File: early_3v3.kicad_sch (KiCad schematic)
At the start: 6 parts, among them U11 SE8633K2-HF

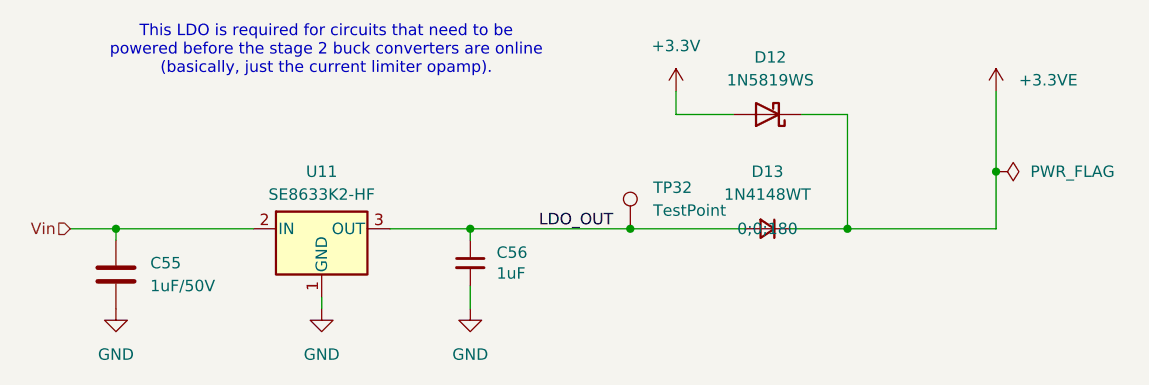
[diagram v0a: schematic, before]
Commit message: Nailed the current limiter design
Also added more GND test pads
Also fixed the MCU I2C pinout
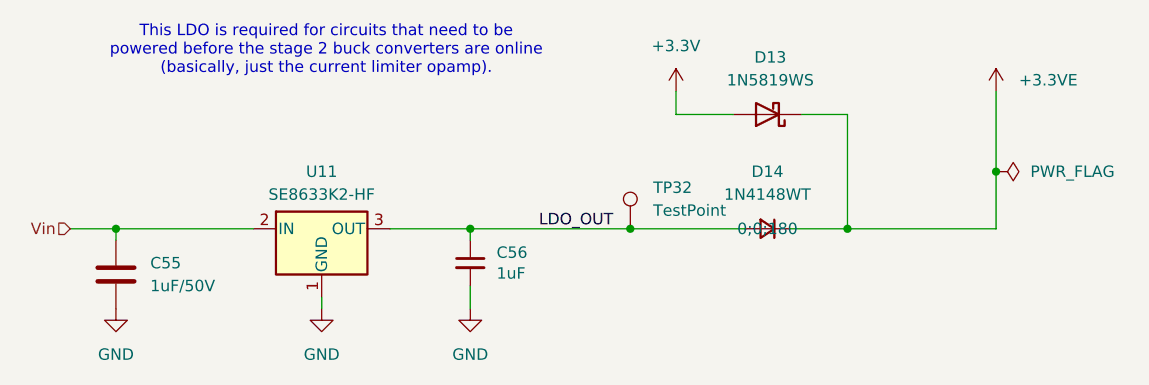
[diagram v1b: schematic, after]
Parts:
- renumbered D12 to D13, D13 to D14
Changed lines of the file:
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@@
 		(dnp no)
 		(fields_autoplaced yes)
-		(property "Reference" "D12"
+		(property "Reference" "D13"
 			(at 193.3575 49.53 0)
 			(effects
@@
 				)
 				(hide yes)
-			)
-		)
-		(property "Field8" ""
-			(at 193.04 55.88 0)
-			(effects
-				(font
-					(size 1.27 1.27)
-				)
-			)
-		)
-		(property "PartNumber" ""
-			(at 193.04 55.88 0)
-			(effects
-				(font
-					(size 1.27 1.27)
-				)
 			)
 		)
@@
 			(project "HALPI2"
 				(path "/abc482bd-3f17-4d35-80db-1da3dcdb5c27/c7bf4e1f-6bd1-4be7-9e56-1bd438bf5d42/8e6a478f-fb3c-4be6-a57a-6d17571606cc"
-					(reference "D12")
+					(reference "D13")
 					(unit 1)
 				)
@@
 		(dnp no)
 		(fields_autoplaced yes)
-		(property "Reference" "D13"
+		(property "Reference" "D14"
 			(at 193.04 62.23 0)
 			(effects
@@
 				)
 				(hide yes)
-			)
-		)
-		(property "LCSC Part" ""
-			(at 193.04 68.58 0)
-			(effects
-				(font
-					(size 1.27 1.27)
-				)
-			)
-		)
-		(property "Field8" ""
-			(at 193.04 68.58 0)
-			(effects
-				(font
-					(size 1.27 1.27)
-				)
-			)
-		)
-		(property "PartNumber" ""
-			(at 193.04 68.58 0)
-			(effects
-				(font
-					(size 1.27 1.27)
-				)
 			)
 		)
@@
 			(project "HALPI2"
 				(path "/abc482bd-3f17-4d35-80db-1da3dcdb5c27/c7bf4e1f-6bd1-4be7-9e56-1bd438bf5d42/8e6a478f-fb3c-4be6-a57a-6d17571606cc"
-					(reference "D13")
+					(reference "D14")
 					(unit 1)
 				)
@@
 			)
 		)
-		(property "LCSC Part" ""
-			(at 120.65 73.66 0)
-			(effects
-				(font
-					(size 1.27 1.27)
-				)
-			)
-		)
-		(property "Field8" ""
-			(at 120.65 73.66 0)
-			(effects
-				(font
-					(size 1.27 1.27)
-				)
-			)
-		)
-		(property "PartNumber" ""
-			(at 120.65 73.66 0)
-			(effects
-				(font
-					(size 1.27 1.27)
-				)
-			)
-		)
 		(pin "1"
 		)
@@
 			)
 		)
-		(property "Field8" ""
-			(at 160.02 72.39 0)
-			(effects
-				(font
-					(size 1.27 1.27)
-				)
-			)
-		)
-		(property "PartNumber" ""
-			(at 160.02 72.39 0)
-			(effects
-				(font
-					(size 1.27 1.27)
-				)
-			)
-		)
 		(pin "1"
 		)
@@
 			)
 		)
-		(property "Field8" ""
-			(at 143.51 68.58 0)
-			(effects
-				(font
-					(size 1.27 1.27)
-				)
-			)
-		)
-		(property "PartNumber" ""
-			(at 143.51 68.58 0)
-			(effects
-				(font
-					(size 1.27 1.27)
-				)
-			)
-		)

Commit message: Final chores
- Reannotate components
- Improve USB2 connector skew matching
- Update sheet blocks
- Fix some diff-pair double-inversions
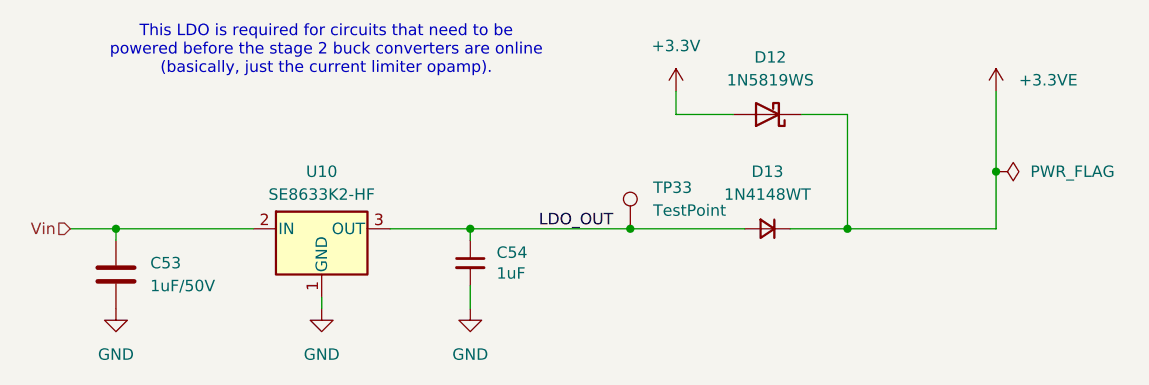
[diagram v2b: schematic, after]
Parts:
- renumbered C55 to C53, C56 to C54, D13 to D12, D14 to D13, TP32 to TP33, U11 to U10
